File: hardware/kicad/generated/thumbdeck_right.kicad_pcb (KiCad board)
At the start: 4 copper layers, 79.5 x 97 mm, 113 parts, among them J1 USB-C, J2 FFC16, J3 JST-PH-2, SW1 SNAP7, SW10 SNAP7, SW11 SNAP7, SW12 SNAP7, SW13 SNAP7, SW14 SNAP7, SW15 SNAP7, SW16 SNAP7, SW17 SNAP7, SW18 SNAP7, SW19 SNAP7, SW2 SNAP7, SW20 SNAP7, SW21 SNAP7, SW22 SNAP7, SW23 SNAP7, SW24 SNAP7, SW25 SNAP7, SW26 SNAP7, SW27 SNAP7, SW28 SNAP7, SW29 SNAP7, SW3 SNAP7, SW30 SNAP7, SW31 SNAP7, SW32 SNAP7, SW33 SNAP7, SW34 SNAP7, SW35 SNAP7, SW36 SNAP7, SW37 SNAP7, SW4 SNAP7, SW5 SNAP7, SW6 SNAP7, SW7 SNAP7, SW8 SNAP7, SW9 SNAP7, SW90 MSK12C02, SW91 TS-1187A, U1 E73-2G4M08S1C, U2 MCP73831, U3 USBLC6-2SC6

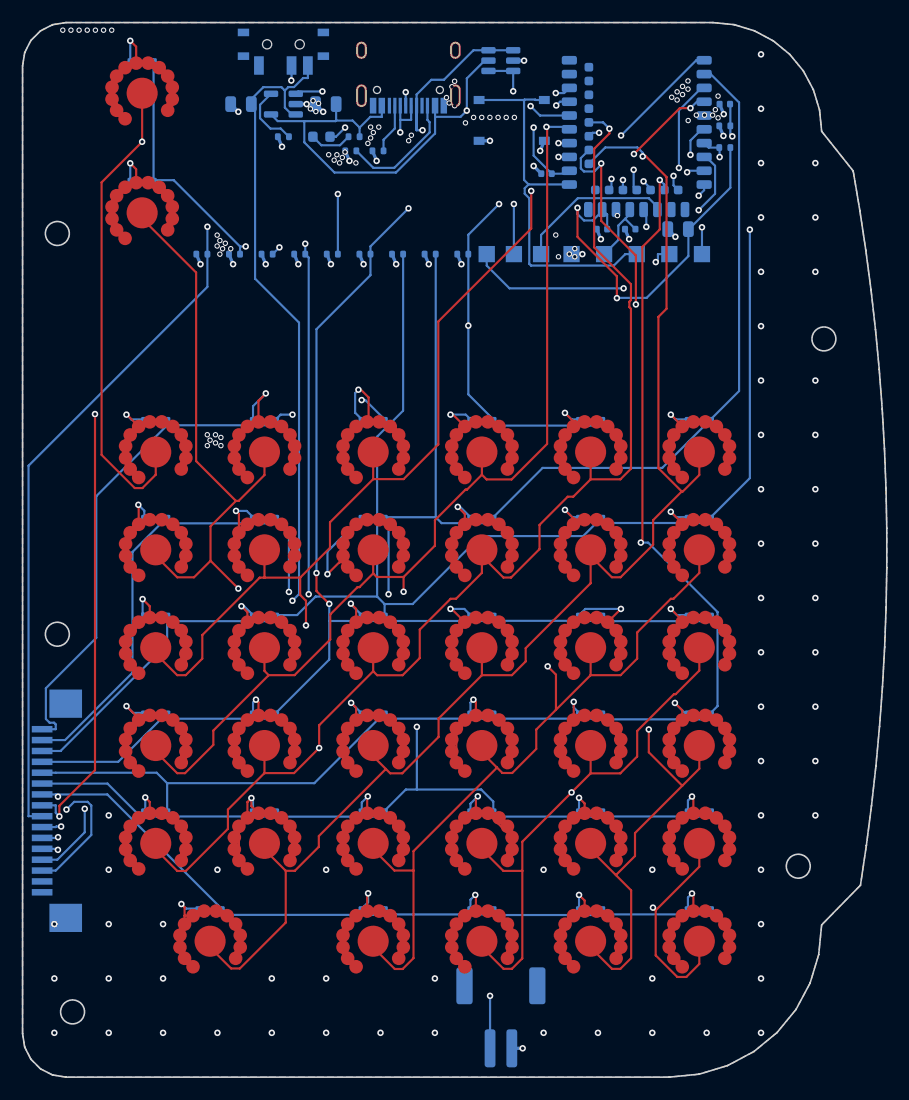
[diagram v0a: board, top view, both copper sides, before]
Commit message: v0.16-follow: Rii-style 2u Enter, keycap legends, M2 screws in the model
Layout (per the Rii i8+ reference, minus the crossed-out features we don't
carry): the right H-row is now H J K L + a DOUBLE-WIDE Enter at the outer
end — the apostrophe key gives up its spot and SQT moves to FN+;. Key count
79 -> 78 (right 36 + left 42). deck.py now lays out each side from its OWN
legend grid (WIDE_KEYS drives 2u caps generically).

Right board regenerated + rerouted: DRC 0 violations / 0 unconnected; fab
package re-exported (67 placements, D1-D36). Left board untouched (0/0).
Firmware regenerated: 78-key transform, SQT on FN+;. sim_matrix PASS.

3D model: 10x M2x10 pan-head screws modeled top-in through the lids (PCB
fit solid gets real mount holes; 0 mm^3 screw/board intersection), and the
keymats carry 0.4mm debossed Rii-style legends (primary + ANSI shifted
secondaries + FN-layer legends; blank space bar, arrow-glyph Backspace,
triangle D-pad). Fit-check: 211 bodies, 0 clashes. GLB + renders + STLs
regenerated; docs swept to 78 keys.

Co-Authored-By: Claude Fable 5 <noreply@anthropic.com>
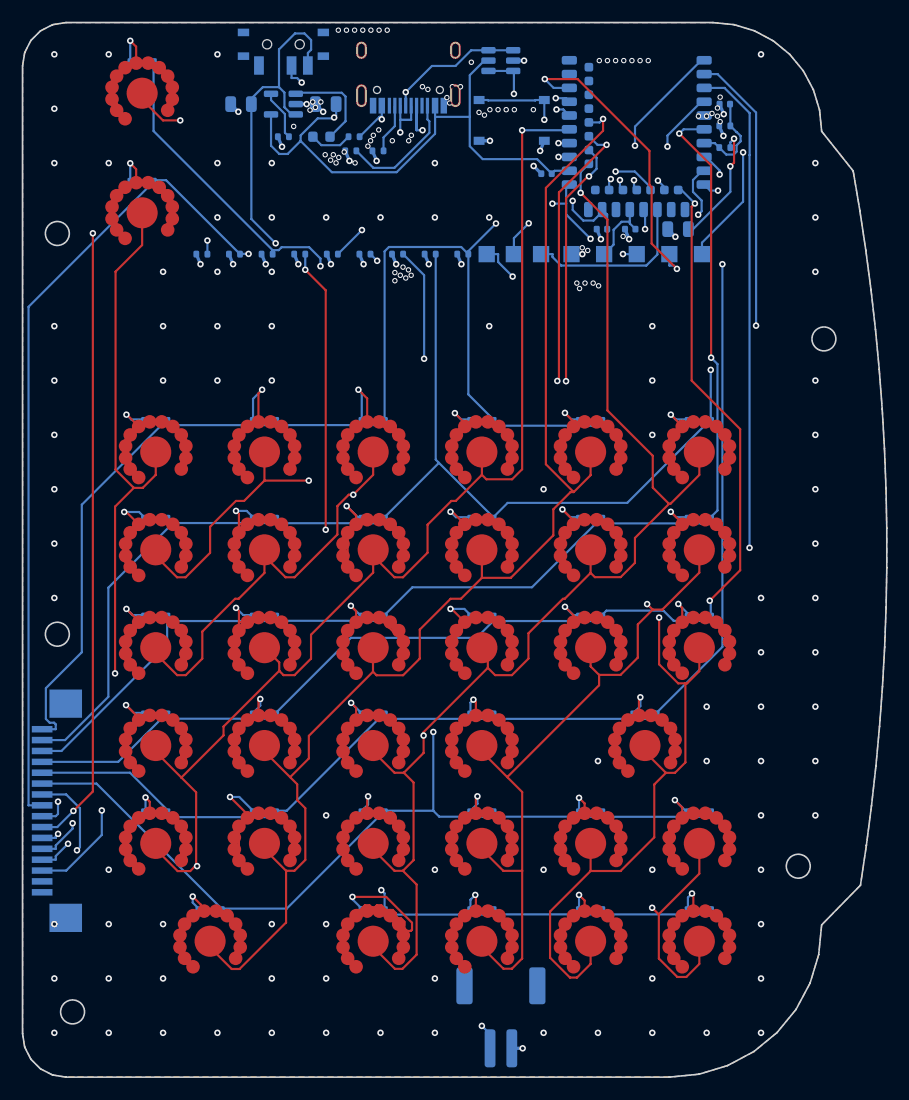
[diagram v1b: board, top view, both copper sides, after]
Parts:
- removed D37: 1N4148WS, D_SOD-323
- removed SW37: SNAP7, snaptron_7mm_contact
- moved D35 93.3 mm to (11.0, 3.50)
- moved SW35 93.3 mm to (11.0, 6.50)
- moved D24 50.8 mm to (12.2, 72.5)
- moved SW24 50.8 mm to (12.2, 75.5)
- moved D30 45.9 mm to (17.2, 81.5)
- moved SW30 45.9 mm to (17.2, 84.5)
- moved D31 15.0 mm to (32.2, 81.5)
- moved SW31 15.0 mm to (32.2, 84.5)
- moved D36 11.0 mm to (11.0, 14.5)
- moved SW36 11.0 mm to (11.0, 17.5)
- moved D25 10.0 mm to (22.2, 72.5)
- moved D26 10.0 mm to (32.2, 72.5)
- moved D27 10.0 mm to (42.2, 72.5)
- moved D28 10.0 mm to (52.2, 72.5)
- moved D29 10.0 mm to (62.2, 72.5)
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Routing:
- net COL1: track 207.4 -> 157.7 mm
- net VBAT_CELL: track 107.2 -> 144.8 mm
- net ROW6: track 164.1 -> 197.6 mm, vias 3 -> 4
- net COL0: track 221.8 -> 196.9 mm, vias 2 -> 3
- net COL8: track 92.7 -> 115.0 mm
- net COL6: track 100.1 -> 121.4 mm
- net COL2: track 166.6 -> 185.4 mm
- net DN_R37: track 17.4 -> 0.00 mm, vias 1 -> 0
- net ROW1: track 154.0 -> 140.5 mm
- net USB_DP: track 45.6 -> 58.4 mm
- net DN_R31: track 17.2 -> 29.8 mm
- net COL3: track 160.7 -> 172.2 mm
- net USB_DM: track 59.5 -> 48.2 mm
- net ROW0: track 126.4 -> 137.3 mm, vias 5 -> 2
- net ROW5: track 155.4 -> 166.3 mm
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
